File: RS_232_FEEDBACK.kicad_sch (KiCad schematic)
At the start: 54 parts, among them IC1 MAX11337ATJ+, J26 RS_232, J29 SPARE_ADC, SW1 SW_SPDT, U6 MAX3232CDR

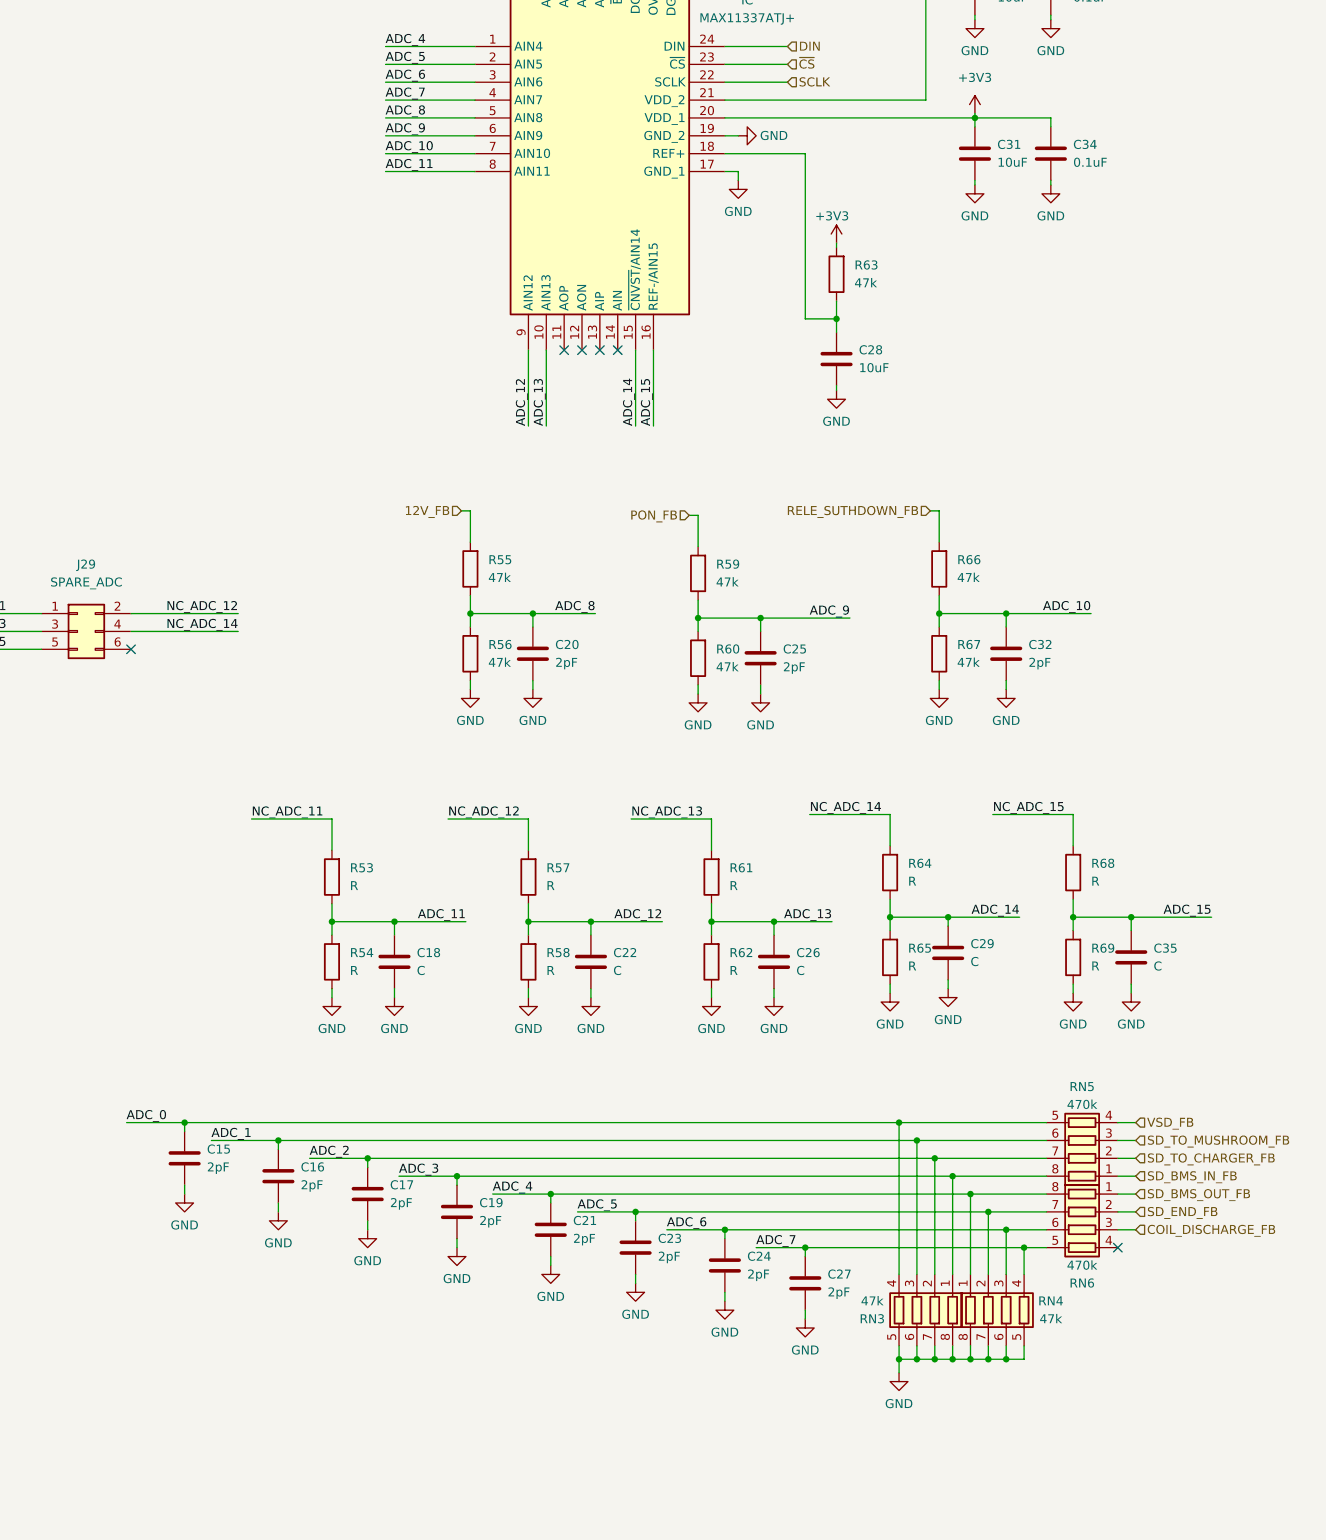
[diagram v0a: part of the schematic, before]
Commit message: Fixed frequency of LPF, added reverse polarity protection
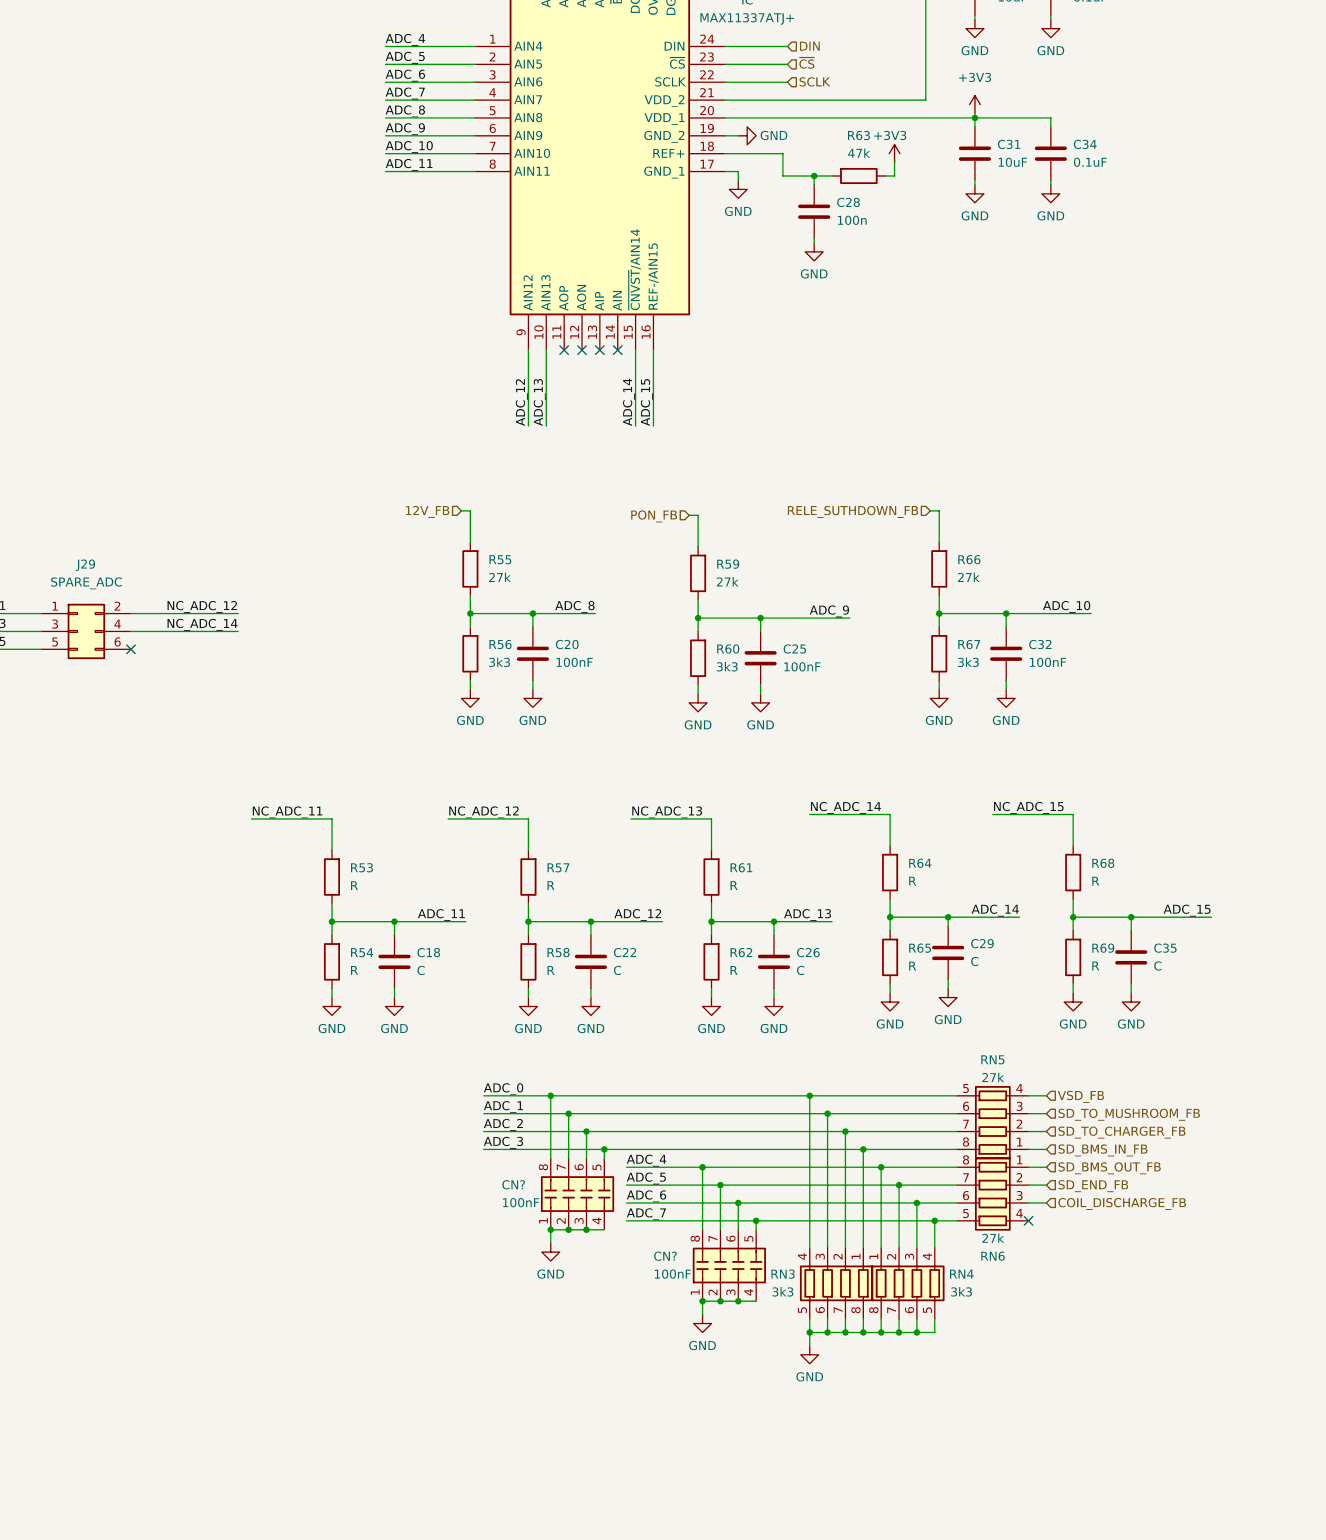
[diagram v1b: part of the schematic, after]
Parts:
- removed C15, C16, C17, C19, C21, C23, C24, C27: 2pF, Resistor_SMD:R_0603_1608Metric, symbol Device:C
- added CN? (x2): 100nF, symbol Eagle_Main:C_Pack04
- C20, C25, C32: value 2pF -> 100nF
- C28: value 10uF -> 100n
- R55, R59, R66: value 47k -> 27k
- R56, R60, R67, RN3, RN4: value 47k -> 3k3
- RN5, RN6: value 470k -> 27k
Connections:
- net +3V3: now also R63.1; no longer R63.2
- net ADC_0: now also CN?.8 (R1.2)
- net ADC_1: now also CN?.7 (R2.2)
- net ADC_2: now also CN?.6 (R3.2)
- net ADC_3: now also CN?.5 (R4.2)
- net ADC_4: now also CN?.8 (R1.2)
- net ADC_5: now also CN?.7 (R2.2)
- net ADC_6: now also CN?.6 (R3.2)
- net ADC_7: now also CN?.5 (R4.2)
- net GND: now also CN?.1 (R1.1), CN?.1 (R1.1), CN?.2 (R2.1), CN?.2 (R2.1), CN?.3 (R3.1), CN?.3 (R3.1), CN?.4 (R4.1), CN?.4 (R4.1)
- net at C28.1, IC1.18 (REF+): now also R63.2; no longer R63.1
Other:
- moved on the sheet: C28, R63, RN3, RN4, RN5, RN6

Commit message: First version of the pcb layout
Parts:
- CN1, CN2: renamed from CN?; footprint (none) -> Resistor_SMD:R_Array_Concave_4x0603
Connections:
- net +3.3V is gone; now on net +3V3: C7.1, R36.1, R37.1, U6.16 (VCC)
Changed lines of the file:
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@@
   (junction (at 285.75 234.95) (diameter 0) (color 0 0 0 0)
   )
+  (junction (at 36.195 83.82) (diameter 0) (color 0 0 0 0)
+  )
   (junction (at 224.79 132.715) (diameter 0) (color 0 0 0 0)
   )
@@
   )
   (junction (at 241.3 220.345) (diameter 0) (color 0 0 0 0)
-  )
-  (junction (at 36.195 83.82) (diameter 0) (color 0 0 0 0)
   )
   (junction (at 259.08 176.53) (diameter 0) (color 0 0 0 0)
@@
     (stroke (width 0) (type default) (color 0 0 0 0))
   )
+  (wire (pts (xy 36.195 83.82) (xy 38.735 83.82))
+    (stroke (width 0) (type default) (color 0 0 0 0))
+  )
   (wire (pts (xy 278.13 233.045) (xy 278.13 234.95))
     (stroke (width 0) (type default) (color 0 0 0 0))
@@
     (stroke (width 0) (type default) (color 0 0 0 0))
   )
-  (wire (pts (xy 36.195 83.82) (xy 33.655 83.82))
-    (stroke (width 0) (type default) (color 0 0 0 0))
-  )
   (wire (pts (xy 291.465 142.24) (xy 291.465 143.51))
     (stroke (width 0) (type default) (color 0 0 0 0))
@@
     (stroke (width 0) (type default) (color 0 0 0 0))
   )
-  (wire (pts (xy 38.735 83.82) (xy 36.195 83.82))
+  (wire (pts (xy 33.655 83.82) (xy 36.195 83.82))
     (stroke (width 0) (type default) (color 0 0 0 0))
   )
@@
     (pin "1")
     (pin "2")
-  )
-  (symbol (lib_id "power:+3.3V") (at 36.195 83.82 0) (mirror y) (unit 1)
-    (in_bom yes) (on_board yes)
-    (property "Reference" "#PWR076" (id 0) (at 36.195 87.63 0)
-      (effects (font (size 1.27 1.27)) hide)
-    )
-    (property "Value" "+3.3V" (id 1) (at 35.814 79.4258 0))
-    (property "Footprint" "" (id 2) (at 36.195 83.82 0)
-      (effects (font (size 1.27 1.27)) hide)
-    )
-    (property "Datasheet" "" (id 3) (at 36.195 83.82 0)
-      (effects (font (size 1.27 1.27)) hide)
-    )
-    (pin "1")
   )
   (symbol (lib_id "Device:C") (at 233.68 138.43 0) (unit 1)
@@
     (pin "1")
   )
+  (symbol (lib_id "power:+3V3") (at 36.195 83.82 0) (unit 1)
+    (in_bom yes) (on_board yes)
+    (property "Reference" "#PWR0150" (id 0) (at 36.195 87.63 0)
+      (effects (font (size 1.27 1.27)) hide)
+    )
+    (property "Value" "+3V3" (id 1) (at 35.56 80.01 0))
+    (property "Footprint" "" (id 2) (at 36.195 83.82 0)
+      (effects (font (size 1.27 1.27)) hide)
+    )
+    (property "Datasheet" "" (id 3) (at 36.195 83.82 0)
+      (effects (font (size 1.27 1.27)) hide)
+    )
+    (pin "1")
+  )
   (symbol (lib_id "Device:R") (at 224.79 126.365 180) (unit 1)
     (in_bom yes) (on_board yes) (fields_autoplaced)
@@
     (pin "1")
   )
+  (symbol (lib_id "power:+3V3") (at 62.865 50.165 0) (unit 1)
+    (in_bom yes) (on_board yes)
+    (property "Reference" "#PWR0149" (id 0) (at 62.865 53.975 0)
+      (effects (font (size 1.27 1.27)) hide)
+    )
+    (property "Value" "+3V3" (id 1) (at 62.23 46.355 0))
+    (property "Footprint" "" (id 2) (at 62.865 50.165 0)
+      (effects (font (size 1.27 1.27)) hide)
+    )
+    (property "Datasheet" "" (id 3) (at 62.865 50.165 0)
+      (effects (font (size 1.27 1.27)) hide)
+    )
+    (pin "1")
+  )
   (symbol (lib_id "power:GND") (at 257.81 232.41 0) (unit 1)
     (in_bom yes) (on_board yes) (fields_autoplaced)
-    (property "Reference" "#PWR?" (id 0) (at 257.81 238.76 0)
+    (property "Reference" "#PWR0137" (id 0) (at 257.81 238.76 0)
       (effects (font (size 1.27 1.27)) hide)
     )
@@
   (symbol (lib_id "power:GND") (at 236.22 222.25 0) (unit 1)
     (in_bom yes) (on_board yes) (fields_autoplaced)
-    (property "Reference" "#PWR?" (id 0) (at 236.22 228.6 0)
+    (property "Reference" "#PWR0140" (id 0) (at 236.22 228.6 0)
       (effects (font (size 1.27 1.27)) hide)
     )
@@
     (pin "1")
     (pin "2")
-  )
-  (symbol (lib_id "power:+3.3V") (at 62.865 50.165 0) (mirror y) (unit 1)
-    (in_bom yes) (on_board yes)
-    (property "Reference" "#PWR078" (id 0) (at 62.865 53.975 0)
-      (effects (font (size 1.27 1.27)) hide)
-    )
-    (property "Value" "+3.3V" (id 1) (at 62.484 45.7708 0))
-    (property "Footprint" "" (id 2) (at 62.865 50.165 0)
-      (effects (font (size 1.27 1.27)) hide)
-    )
-    (property "Datasheet" "" (id 3) (at 62.865 50.165 0)
-      (effects (font (size 1.27 1.27)) hide)
-    )
-    (pin "1")
   )
   (symbol (lib_id "power:GND") (at 284.48 186.69 0) (unit 1)
@@
   (symbol (lib_id "Eagle_Main:C_Pack04") (at 241.3 215.265 0) (unit 1)
     (in_bom yes) (on_board yes)
-    (property "Reference" "CN?" (id 0) (at 229.235 213.995 0)
+    (property "Reference" "CN1" (id 0) (at 229.235 213.995 0)
       (effects (font (size 1.27 1.27)) (justify left))
     )
@@
       (effects (font (size 1.27 1.27)) (justify left))
     )
-    (property "Footprint" "" (id 2) (at 248.285 215.265 90)
+    (property "Footprint" "Resistor_SMD:R_Array_Concave_4x0603" (id 2) (at 248.285 215.265 90)
       (effects (font (size 1.27 1.27)) hide)
     )
@@
   (symbol (lib_id "Eagle_Main:C_Pack04") (at 262.89 225.425 0) (unit 1)
     (in_bom yes) (on_board yes)
-    (property "Reference" "CN?" (id 0) (at 250.825 224.155 0)
+    (property "Reference" "CN2" (id 0) (at 250.825 224.155 0)
       (effects (font (size 1.27 1.27)) (justify left))
     )
@@
       (effects (font (size 1.27 1.27)) (justify left))
     )
-    (property "Footprint" "" (id 2) (at 269.875 225.425 90)
-      (effects (font (size 1.27 1.27)) hide)
-    )
+    (property "Footprint" "Resistor_SMD:R_Array_Concave_4x0603" (id 2) (at 269.875 225.425 90)
+      (effects (font (size 1.27 1.27)) hide)
+    )

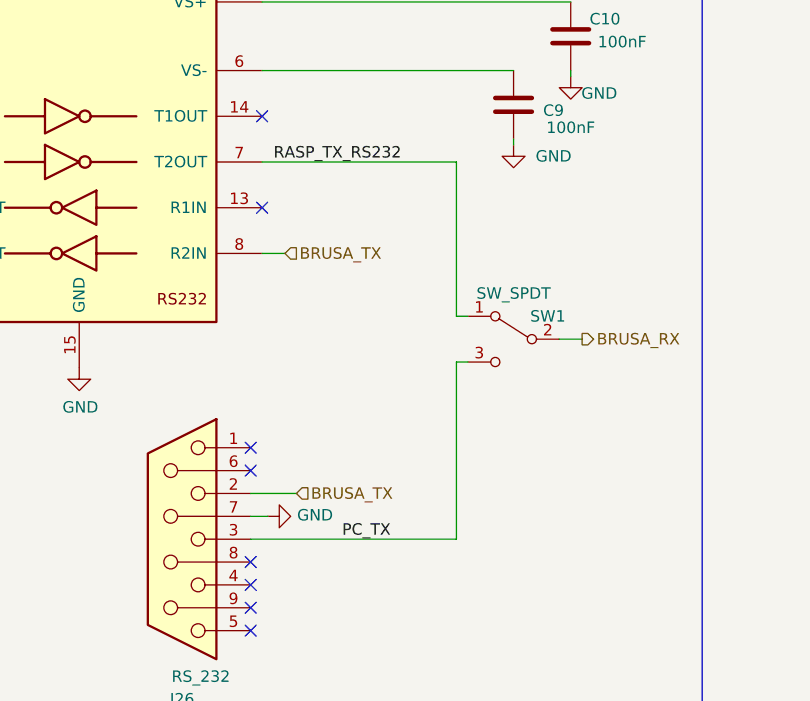
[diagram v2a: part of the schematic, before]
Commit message: Second iteration of the board layout. Need to fix some traces
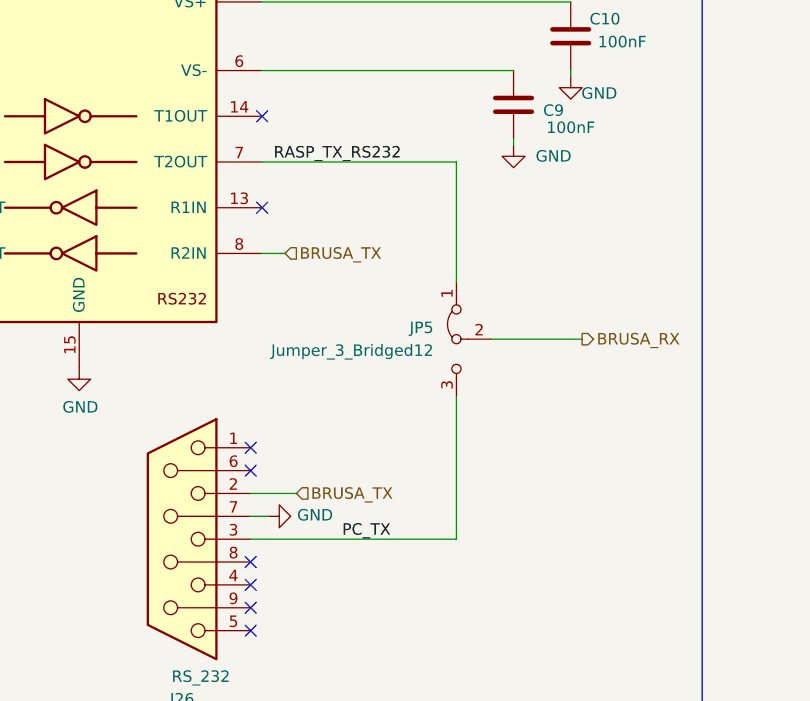
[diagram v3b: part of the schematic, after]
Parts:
- removed SW1: SW_SPDT, Button_Switch_THT:SW_E-Switch_EG1224_SPDT_Angled, symbol Switch:SW_SPDT
- added JP5: Jumper_3_Bridged12, Connector_PinHeader_2.54mm:PinHeader_1x03_P2.54mm_Vertical, symbol Jumper:Jumper_3_Bridged12
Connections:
- net BRUSA_RX: now also JP5.2 (C)
- net PC_TX: now also JP5.3 (B)
- net RASP_TX_RS232: now also JP5.1 (A)
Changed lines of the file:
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@@
-    (stroke (width 0) (type default) (color 0 0 0 0))
-  )
-  (wire (pts (xy 104.775 99.06) (xy 104.775 116.205))
     (stroke (width 0) (type default) (color 0 0 0 0))
   )
@@
     (stroke (width 0) (type default) (color 0 0 0 0))
   )
+  (wire (pts (xy 108.585 118.745) (xy 118.745 118.745))
+    (stroke (width 0) (type default) (color 0 0 0 0))
+  )
   (wire (pts (xy 241.3 206.375) (xy 278.13 206.375))
     (stroke (width 0) (type default) (color 0 0 0 0))
@@
     (stroke (width 0) (type default) (color 0 0 0 0))
   )
-  (wire (pts (xy 116.205 118.745) (xy 118.745 118.745))
-    (stroke (width 0) (type default) (color 0 0 0 0))
-  )
   (wire (pts (xy 284.48 161.29) (xy 284.48 165.735))
     (stroke (width 0) (type default) (color 0 0 0 0))
@@
     (stroke (width 0) (type default) (color 0 0 0 0))
   )
-  (wire (pts (xy 104.775 116.205) (xy 106.045 116.205))
-    (stroke (width 0) (type default) (color 0 0 0 0))
-  )
   (wire (pts (xy 310.515 175.895) (xy 310.515 177.8))
     (stroke (width 0) (type default) (color 0 0 0 0))
@@
     (stroke (width 0) (type default) (color 0 0 0 0))
   )
+  (wire (pts (xy 104.775 99.06) (xy 104.775 112.395))
+    (stroke (width 0) (type default) (color 0 0 0 0))
+  )
   (wire (pts (xy 288.29 234.95) (xy 285.75 234.95))
     (stroke (width 0) (type default) (color 0 0 0 0))
   )
-  (wire (pts (xy 104.775 121.285) (xy 106.045 121.285))
-    (stroke (width 0) (type default) (color 0 0 0 0))
-  )
   (wire (pts (xy 260.985 57.15) (xy 269.875 57.15))
     (stroke (width 0) (type default) (color 0 0 0 0))
@@
     (stroke (width 0) (type default) (color 0 0 0 0))
   )
+  (wire (pts (xy 104.775 125.095) (xy 104.775 140.97))
+    (stroke (width 0) (type default) (color 0 0 0 0))
+  )
   (wire (pts (xy 275.59 203.835) (xy 275.59 222.885))
     (stroke (width 0) (type default) (color 0 0 0 0))
@@
   )
   (wire (pts (xy 27.94 99.06) (xy 33.655 99.06))
-    (stroke (width 0) (type default) (color 0 0 0 0))
-  )
-  (wire (pts (xy 104.775 140.97) (xy 104.775 121.285))
     (stroke (width 0) (type default) (color 0 0 0 0))
   )
@@
     (pin "8")
   )
+  (symbol (lib_id "Jumper:Jumper_3_Bridged12") (at 104.775 118.745 90) (mirror x) (unit 1)
+    (in_bom yes) (on_board yes) (fields_autoplaced)
+    (property "Reference" "JP5" (id 0) (at 102.235 117.4749 90)
+      (effects (font (size 1.27 1.27)) (justify left))
+    )
+    (property "Value" "Jumper_3_Bridged12" (id 1) (at 102.235 120.0149 90)
+      (effects (font (size 1.27 1.27)) (justify left))
+    )
+    (property "Footprint" "Connector_PinHeader_2.54mm:PinHeader_1x03_P2.54mm_Vertical" (id 2) (at 104.775 118.745 0)
+      (effects (font (size 1.27 1.27)) hide)
+    )
+    (property "Datasheet" "~" (id 3) (at 104.775 118.745 0)
+      (effects (font (size 1.27 1.27)) hide)
+    )
+    (pin "1")
+    (pin "2")
+    (pin "3")
+  )
   (symbol (lib_id "power:GND") (at 233.68 143.51 0) (unit 1)
     (in_bom yes) (on_board yes) (fields_autoplaced)
@@
     (pin "9")
   )
-  (symbol (lib_id "Switch:SW_SPDT") (at 111.125 118.745 0) (mirror y) (unit 1)
-    (in_bom yes) (on_board yes)
-    (property "Reference" "SW1" (id 0) (at 114.935 116.205 0))
-    (property "Value" "SW_SPDT" (id 1) (at 111.125 113.665 0))
-    (property "Footprint" "Button_Switch_THT:SW_E-Switch_EG1224_SPDT_Angled" (id 2) (at 111.125 118.745 0)
-      (effects (font (size 1.27 1.27)) hide)
-    )
-    (property "Datasheet" "~" (id 3) (at 111.125 118.745 0)
-      (effects (font (size 1.27 1.27)) hide)
-    )
-    (pin "1")
-    (pin "2")
-    (pin "3")
-  )
   (symbol (lib_id "power:GND") (at 117.475 89.535 0) (unit 1)
